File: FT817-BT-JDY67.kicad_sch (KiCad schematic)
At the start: 27 parts, among them J1009 Mini-DIN-8PR, J1010 Mini-DIN-6PR, U1 JDY-67 Bluetooth Module, U2 LM1117MP-3.3

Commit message: update
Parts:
- R8: footprint (none) -> Resistor_SMD:R_0805_2012Metric
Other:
- note added: "Audio Out Volume"
- note added: "Mic Volume"
- company: BG6LH -> https://github.com/BG6LH/FT-81x-BT-DIGI-Adaptor
- moved on the sheet: C3
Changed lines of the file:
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@@
     (date "2023-05-17")
     (rev "20230517")
-    (company "BG6LH")
+    (company "https://github.com/BG6LH/FT-81x-BT-DIGI-Adaptor")
     (comment 1 "CC-BY-NC-SA 4.0")
     (comment 2 "With special thanks to: BG6JJI, BI1EIH")
@@
     (stroke (width 0) (type default))
   )
-  (wire (pts (xy 207.01 121.92) (xy 212.09 121.92))
+  (wire (pts (xy 207.01 121.92) (xy 213.36 121.92))
     (stroke (width 0) (type default))
   )
@@
     (stroke (width 0) (type default))
   )
-  (wire (pts (xy 219.71 121.92) (xy 227.33 121.92))
+  (wire (pts (xy 220.98 121.92) (xy 227.33 121.92))
     (stroke (width 0) (type default))
   )
@@
     (at 25.4 33.02 0)
     (effects (font (size 2 2)) (justify left bottom))
+  )
+  (text "Mic Volume" (at 193.04 127 0)
+    (effects (font (size 1.27 1.27)) (justify left bottom))
+  )
+  (text "Audio Out Volume" (at 203.2 147.32 0)
+    (effects (font (size 1.27 1.27)) (justify left bottom))
   )
   (global_label "3.3V" (shape input) (at 114.3 129.54 180) (fields_autoplaced)
@@
     )
   )
-  (symbol (lib_id "Device:C") (at 215.9 121.92 90) (unit 1)
+  (symbol (lib_id "Device:C") (at 217.17 121.92 90) (unit 1)
     (in_bom yes) (on_board yes) (dnp no)
-    (property "Reference" "C3" (at 215.9 115.57 90)
-      (effects (font (size 1.27 1.27)))
-    )
-    (property "Value" "1uF" (at 215.9 118.11 90)
-      (effects (font (size 1.27 1.27)))
-    )
-    (property "Footprint" "Capacitor_SMD:C_0805_2012Metric" (at 219.71 120.9548 0)
-      (effects (font (size 1.27 1.27)) hide)
-    )
-    (property "Datasheet" "~" (at 215.9 121.92 0)
+    (property "Reference" "C3" (at 217.17 115.57 90)
+      (effects (font (size 1.27 1.27)))
+    )
+    (property "Value" "1uF" (at 217.17 118.11 90)
+      (effects (font (size 1.27 1.27)))
+    )
+    (property "Footprint" "Capacitor_SMD:C_0805_2012Metric" (at 220.98 120.9548 0)
+      (effects (font (size 1.27 1.27)) hide)
+    )
+    (property "Datasheet" "~" (at 217.17 121.92 0)
       (effects (font (size 1.27 1.27)) hide)
     )
@@
       (effects (font (size 1.27 1.27)))
     )
-    (property "Footprint" "" (at 203.2 123.698 90)
-      (effects (font (size 1.27 1.27)) hide)
-    )
+    (property "Footprint" "Resistor_SMD:R_0805_2012Metric" (at 203.2 123.698 90)
+      (effects (font (size 1.27 1.27)) hide)
+    )

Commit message: minimal update
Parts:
- R3, R4: value 22 -> 22R
- R6: value 50R -> 51R
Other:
- note added: "RXD Audio Volume"
- note added: "TX Audio Volume"
- note removed: "Audio Out Volume"
- note removed: "Mic Volume"
- title: FT-81x BT  DIGI Adaptor -> FT-81x BT DIGI Adaptor
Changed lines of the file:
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@@
   (paper "A4")
   (title_block
-    (title "FT-81x BT  DIGI Adaptor")
-    (date "2023-05-17")
-    (rev "20230517")
+    (title "FT-81x BT DIGI Adaptor")
+    (date "2023-05-22")
+    (rev "20230522")
     (company "https://github.com/BG6LH/FT-81x-BT-DIGI-Adaptor")
     (comment 1 "CC-BY-NC-SA 4.0")
@@
     (effects (font (size 2 2)) (justify left bottom))
   )
-  (text "Mic Volume" (at 193.04 127 0)
+  (text "RXD Audio Volume" (at 193.04 127 0)
     (effects (font (size 1.27 1.27)) (justify left bottom))
   )
-  (text "Audio Out Volume" (at 203.2 147.32 0)
+  (text "TX Audio Volume" (at 203.2 147.32 0)
     (effects (font (size 1.27 1.27)) (justify left bottom))
   )
@@
       (effects (font (size 1.27 1.27)))
     )
-    (property "Value" "22" (at 114.3 104.14 90)
+    (property "Value" "22R" (at 114.3 104.14 90)
       (effects (font (size 1.27 1.27)))
     )
@@
       (effects (font (size 1.27 1.27)))
     )
-    (property "Value" "22" (at 114.3 96.52 90)
+    (property "Value" "22R" (at 114.3 96.52 90)
       (effects (font (size 1.27 1.27)))
     )
@@
       (effects (font (size 1.27 1.27)))
     )
-    (property "Value" "50R" (at 175.26 48.26 90)
-      (effects (font (size 1.27 1.27)))
-    )
+    (property "Value" "51R" (at 175.26 48.26 90)
+      (effects (font (size 1.27 1.27)))
+    )

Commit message: update
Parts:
- C1, C2: symbol Device:C_Polarized -> FT81x-BT_DIGI-Adapter_Library:C_Polarized
- C3, C4, C5, C6: symbol Device:C -> FT81x-BT_DIGI-Adapter_Library:C
- D1, D2: symbol Device:LED -> FT81x-BT_DIGI-Adapter_Library:LED
- D4: symbol Device:D_Zener -> FT81x-BT_DIGI-Adapter_Library:D_Zener
- H1, H2: symbol Mechanical:MountingHole_Pad -> FT81x-BT_DIGI-Adapter_Library:MountingHole_Pad
- H3: footprint BG6LH_Kicad_Libary:FT-817_GND_terminal_8.4mm_M8_Pad_TopBottom -> FT81x-BT-DIGI-Adapter-Library:FT-817_GND_terminal_8.4mm_M8_Pad_TopBottom; symbol Mechanical:MountingHole_Pad -> FT81x-BT_DIGI-Adapter_Library:MountingHole_Pad
- J1009: footprint BG6LH_MiniDin_Pin:MD-8Pin -> FT81x-BT-DIGI-Adapter-Library:MD-8Pin_Reverse; symbol Connector:Mini-DIN-8 -> FT81x-BT_DIGI-Adapter_Library:Mini-DIN-8PR
- J1010: footprint BG6LH_MiniDin_Pin:MD-6Pin -> FT81x-BT-DIGI-Adapter-Library:MD-6Pin_Reverse; symbol Connector:Mini-DIN-6 -> FT81x-BT_DIGI-Adapter_Library:Mini-DIN-6PR
- L1, L2: symbol Device:L_Ferrite -> FT81x-BT_DIGI-Adapter_Library:L_Ferrite
- R1, R2, R3, R4, R7, R8: symbol Device:R -> FT81x-BT_DIGI-Adapter_Library:R
- R6: value 51R -> 270R; symbol Device:R -> FT81x-BT_DIGI-Adapter_Library:R
- RV1, RV2: symbol Device:R_Potentiometer -> FT81x-BT_DIGI-Adapter_Library:R_Potentiometer
- U1: footprint BG6LH_Kicad_Libary:JDY-67_Bluetooth_Module -> FT81x-BT-DIGI-Adapter-Library:JDY-67_Bluetooth_Module; symbol kicad_lceda:JDY-67蓝牙模块 -> FT81x-BT_DIGI-Adapter_Library:JDY-67_Bluetooth_Module; uuid std:d9fbb221c1a84866ab03cd176b316aa0 -> (none)
- U2: symbol Regulator_Linear:LM1117MP-3.3 -> FT81x-BT_DIGI-Adapter_Library:LM1117MP-3.3
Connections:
- net GND: now also J1009.9 (GND), J1010.7 (GND)

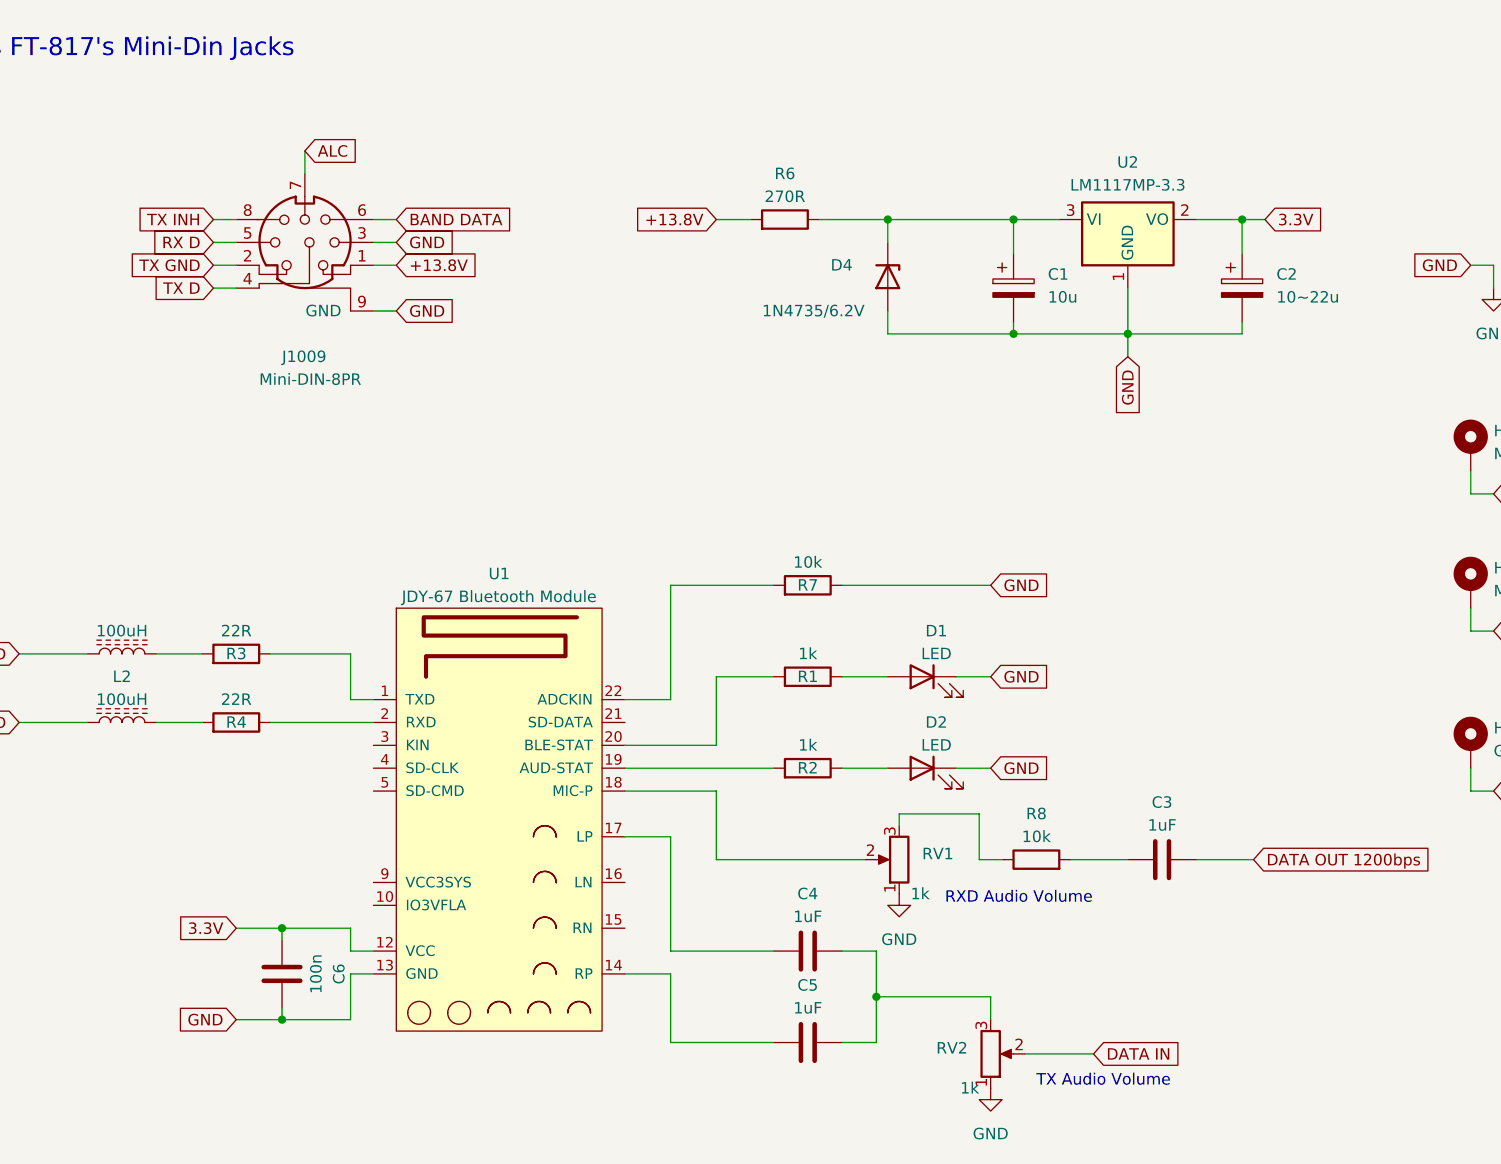
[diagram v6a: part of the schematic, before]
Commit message: Replace VR with fixed resistor. Optimized LDO circuit.
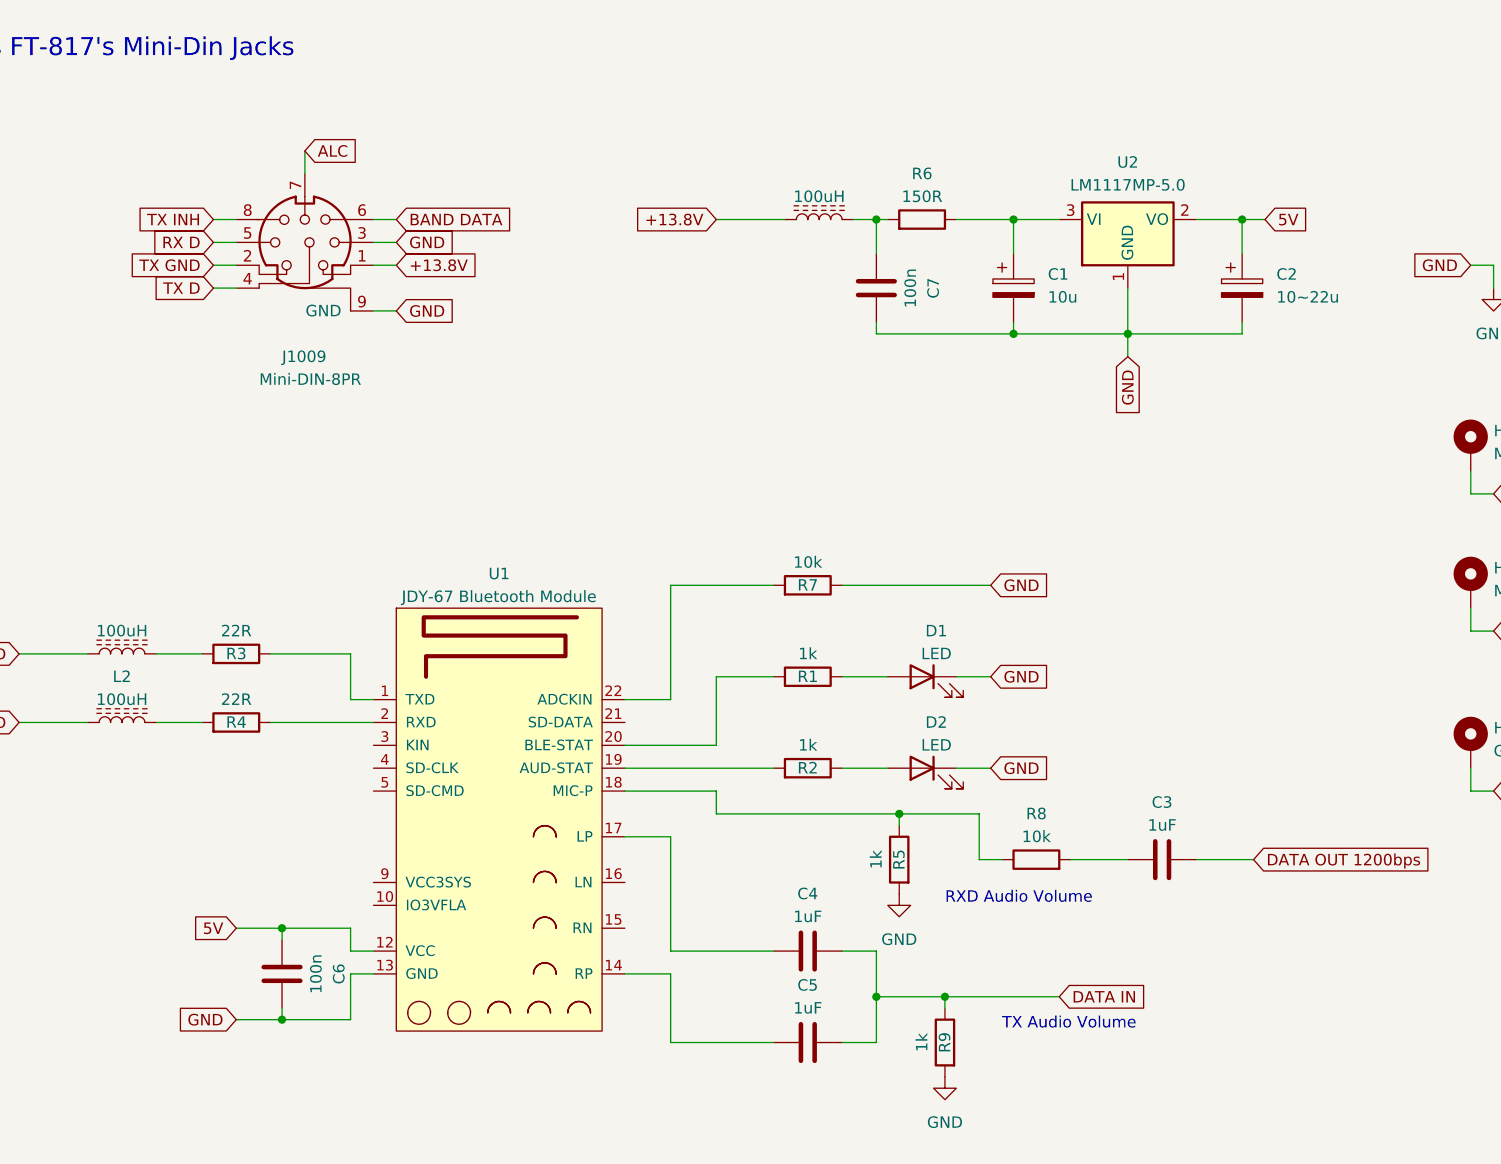
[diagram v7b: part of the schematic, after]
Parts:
- removed D4: 1N4735/6.2V, Diode_SMD:D_SMA, symbol FT81x-BT_DIGI-Adapter_Library:D_Zener
- removed RV1, RV2: 1k, Potentiometer_SMD:Potentiometer_Bourns_3314J_Vertical, symbol FT81x-BT_DIGI-Adapter_Library:R_Potentiometer
- added C7: 100n, Capacitor_SMD:C_0805_2012Metric, symbol FT81x-BT_DIGI-Adapter_Library:C
- added L3: 100uH, Inductor_SMD:L_0805_2012Metric_Pad1.05x1.20mm_HandSolder, symbol FT81x-BT_DIGI-Adapter_Library:L_Ferrite
- added R5, R9: 1k, Resistor_SMD:R_0805_2012Metric, symbol FT81x-BT_DIGI-Adapter_Library:R
- R6: value 270R -> 150R
- U2: value LM1117MP-3.3 -> LM1117MP-5.0
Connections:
- net +13.8V: now also L3.1; no longer R6.2
- net DATA IN: now also C4.2, C5.2, R9.1
- net GND: now also C7.2, R5.2, R9.2
- net at U1.18 (MIC-P): now also R8.1, R5.1
- net 3.3V renamed 5V
- new net: C7.1, L3.2, R6.2
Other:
- moved on the sheet: R6

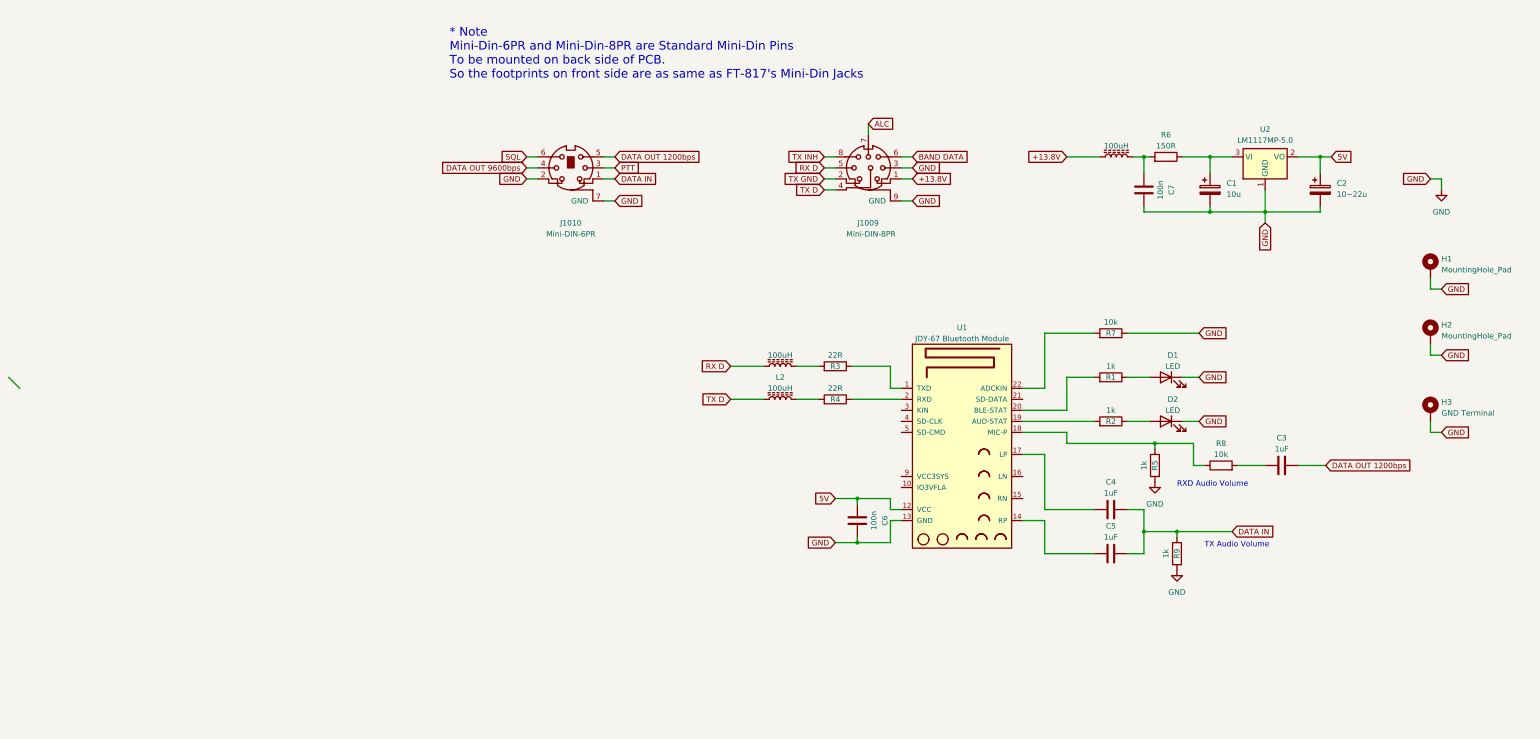
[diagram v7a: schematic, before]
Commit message: Add power shutdown circuit
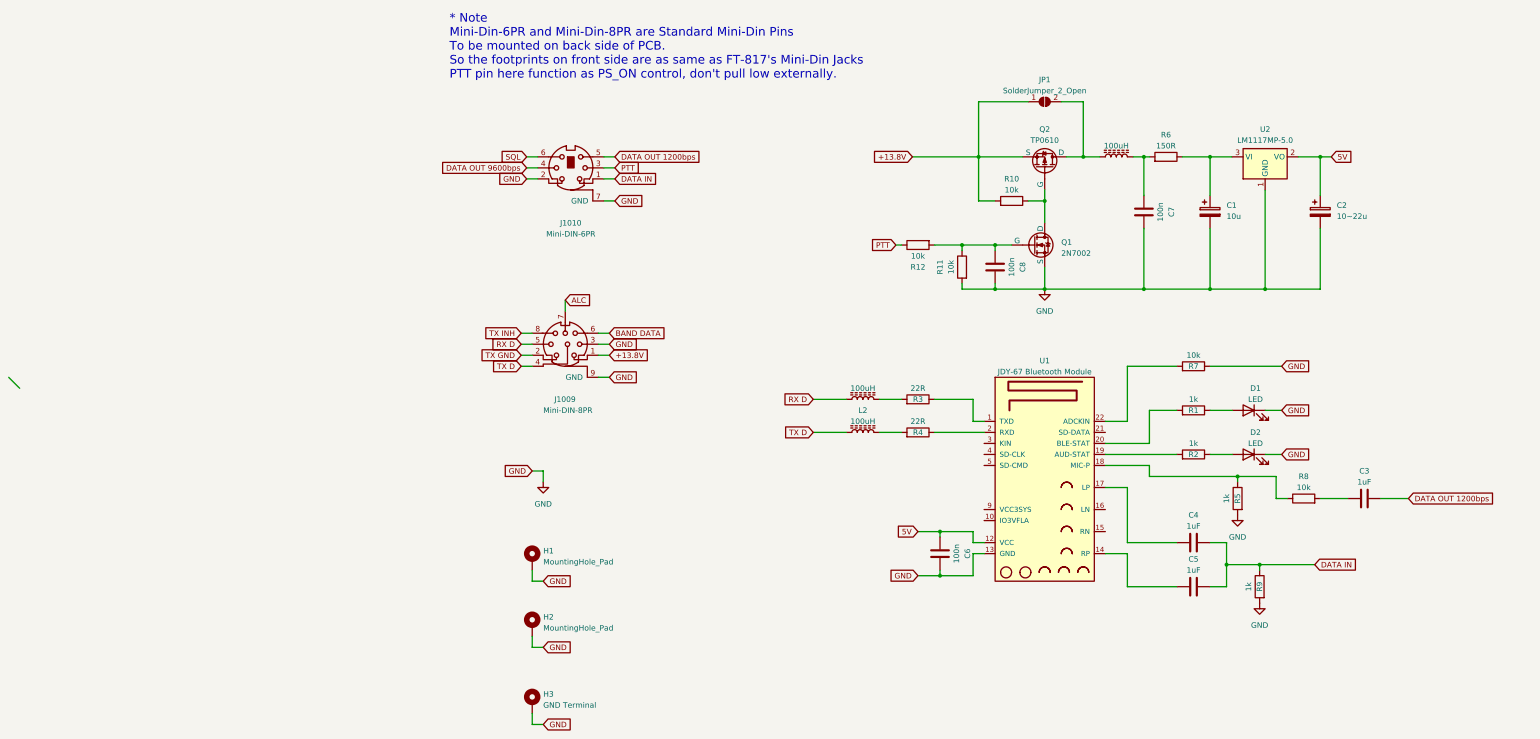
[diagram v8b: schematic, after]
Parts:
- added C8: 100n, Capacitor_SMD:C_0805_2012Metric, symbol FT81x-BT_DIGI-Adapter_Library:C
- added JP1: SolderJumper_2_Open, Jumper:SolderJumper-2_P1.3mm_Open_RoundedPad1.0x1.5mm, symbol Jumper:SolderJumper_2_Open
- added Q1: 2N7002, Package_TO_SOT_SMD:SOT-23-3, symbol Simulation_SPICE:NMOS
- added Q2: TP0610, Package_TO_SOT_SMD:SOT-23-3, symbol Simulation_SPICE:PMOS
- added R10, R11, R12: 10k, Resistor_SMD:R_0805_2012Metric, symbol FT81x-BT_DIGI-Adapter_Library:R
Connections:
- net +13.8V: now also JP1.1 (A), Q2.3 (S), R10.2; no longer L3.1
- net GND: now also C8.2, Q1.3 (S), R11.2
- net PTT: now also R12.1
- new net: C8.1, Q1.2 (G), R11.1, R12.2
- new net: Q1.1 (D), Q2.2 (G), R10.1
- new net: JP1.2 (B), L3.1, Q2.1 (D)
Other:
- note added: "* Note Mini-Din-6PR and Mini-Din-8PR are Standard Mini-Din Pins To be mounted on back side of PCB. So the footprints on front side are as same as FT-817's Mini-Din Jacks PTT pin here function as PS_ON control, don't pull low externally."
- note removed: "* Note Mini-Din-6PR and Mini-Din-8PR are Standard Mini-Din Pins To be mounted on back side of PCB. So the footprints on front side are as same as FT-817's Mini-Din Jacks"
- note removed: "RXD Audio Volume"
- note removed: "TX Audio Volume"
- moved on the sheet: C1, C2, C3, C4, C5, C6, C7, D1, D2, H1, H2, H3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
